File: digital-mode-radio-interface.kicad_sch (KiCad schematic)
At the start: 0 parts

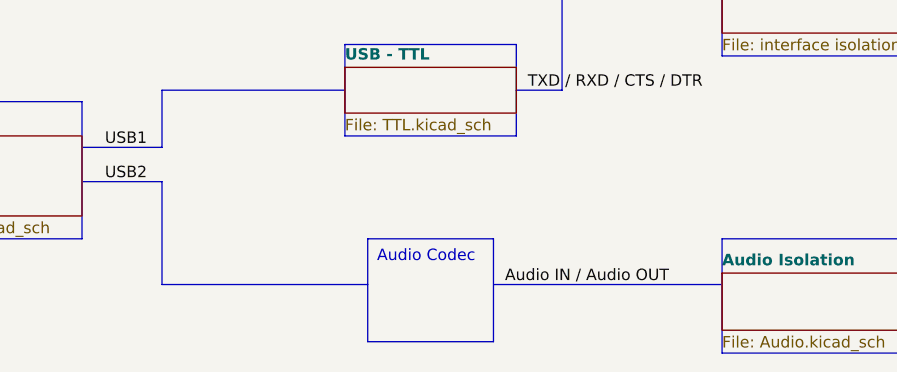
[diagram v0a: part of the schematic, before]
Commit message: Add CM108B codex schematic parts and plumb to USB, and Audio Isolation
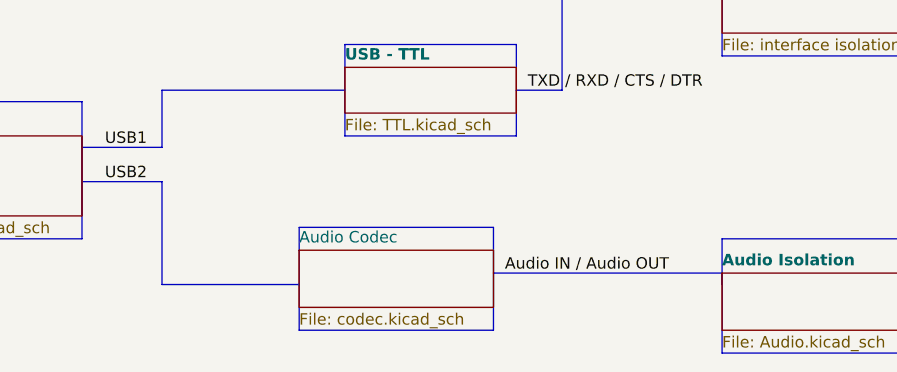
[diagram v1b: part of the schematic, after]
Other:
- added sheet Audio Codec (codec.kicad_sch)
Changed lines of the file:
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@@
 	(polyline
 		(pts
-			(xy 64.77 82.55) (xy 87.63 82.55)
+			(xy 64.77 82.55) (xy 80.01 82.55)
 		)
 		(stroke
@@
 	(polyline
 		(pts
-			(xy 101.6 82.55) (xy 127 82.55)
+			(xy 101.6 81.28) (xy 127 81.28)
 		)
 		(stroke
@@
 		)
 	)
-	(text_box "Audio Codec"
-		(exclude_from_sim no)
-		(at 87.63 77.47 0)
-		(size 13.97 11.43)
+	(text_box ""
+		(exclude_from_sim no)
+		(at 80.01 76.2 0)
+		(size 21.59 11.43)
 		(stroke
 			(width 0)
@@
 	)
 	(label "Audio IN {slash} Audio OUT"
-		(at 102.87 82.55 0)
+		(at 102.87 81.28 0)
 		(fields_autoplaced yes)
 		(effects
@@
 				)
 			)
+		)
+	)
+	(sheet
+		(at 80.01 78.74)
+		(size 21.59 6.35)
+		(fields_autoplaced yes)
+		(stroke
+			(width 0.1524)
+			(type solid)
+		)
+		(fill
+			(color 0 0 0 0.0000)
+		)
+		(property "Sheetname" "Audio Codec"
+			(at 80.01 78.0284 0)
+			(effects
+				(font
+					(size 1.27 1.27)
+				)
+				(justify left bottom)
+			)
+		)
+		(property "Sheetfile" "codec.kicad_sch"
+			(at 80.01 85.6746 0)
+			(effects
+				(font
+					(size 1.27 1.27)
+				)
+				(justify left top)
+			)
+		)
+		(instances
+			(project "digital-mode-radio-interface"
+				(path "/a0d4bcf6-6cac-4e92-853e-9083f008b231"
+					(page "7")
+				)
+			)

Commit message: Move Radio interface onto it's own sheet, Add mounting holes and case outline
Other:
- added sheet Radio Interface (radio_iface.kicad_sch)
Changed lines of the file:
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@@
 	(polyline
 		(pts
-			(xy 173.99 48.26) (xy 173.99 60.96)
+			(xy 179.07 48.26) (xy 179.07 60.96)
 		)
 		(stroke
@@
 	(polyline
 		(pts
-			(xy 160.02 48.26) (xy 173.99 48.26)
+			(xy 160.02 48.26) (xy 179.07 48.26)
 		)
 		(stroke
@@
 	(polyline
 		(pts
-			(xy 147.32 83.82) (xy 173.99 83.82)
+			(xy 147.32 83.82) (xy 179.07 83.82)
 		)
 		(stroke
@@
 	(polyline
 		(pts
-			(xy 173.99 73.66) (xy 173.99 83.82)
+			(xy 179.07 72.39) (xy 179.07 83.82)
 		)
 		(stroke
@@
 		)
 	)
-	(text_box "Radio"
+	(text_box ""
 		(exclude_from_sim no)
 		(at 165.1 60.96 0)
-		(size 17.78 12.7)
+		(size 25.4 11.43)
 		(stroke
 			(width 0)
@@
 				)
 			)
+		)
+	)
+	(sheet
+		(at 165.1 63.5)
+		(size 25.4 6.35)
+		(fields_autoplaced yes)
+		(stroke
+			(width 0.1524)
+			(type solid)
+		)
+		(fill
+			(color 0 0 0 0.0000)
+		)
+		(property "Sheetname" "Radio Interface"
+			(at 165.1 62.7884 0)
+			(effects
+				(font
+					(size 1.27 1.27)
+				)
+				(justify left bottom)
+			)
+		)
+		(property "Sheetfile" "radio_iface.kicad_sch"
+			(at 165.1 70.4346 0)
+			(effects
+				(font
+					(size 1.27 1.27)
+				)
+				(justify left top)
+			)
+		)
+		(instances
+			(project "digital-mode-radio-interface"
+				(path "/a0d4bcf6-6cac-4e92-853e-9083f008b231"
+					(page "8")
+				)
+			)
